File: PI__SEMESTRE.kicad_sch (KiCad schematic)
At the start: 30 parts, among them IC2 LMV358IDR, J1 CX90B-16P1, J3 Conn_01x04, SW1 SW_Boot, SW2 SW_Reset, U1 ESP32-S3-WROOM-1, U2 AMS1117, U5 GUVA-S12SD, U6 BME688

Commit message: cambios realizados para el esp32 s3 y unificacion de hojas
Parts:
- removed C1: TAJA106K016RNJ, TAJA106K016RNJ:CAPPM3216X180N, symbol TAJA106K016RNJ:TAJA106K016RNJ
- removed C2: TCJB226M025R0150E, TCJB226MO025R0150E:CAPPM3528X210N, symbol TCJB226M025R0150E:TCJB226M025R0150E
- added C1: 10u, symbol Device:C
- added C2: 100u, symbol Device:C
- added D2, D3: LED, LED_SMD:LED_1206_3216Metric, symbol Device:LED
- added R8, R9: 5.1KΩ, Resistor_SMD:R_0805_2012Metric, symbol Device:R
- C4: value 0.1uf -> 22u; footprint Capacitor_SMD:C_0201_0603Metric -> (none)
- C5: value 10uf -> 100n; footprint Capacitor_SMD:C_0402_1005Metric -> (none)
- R1, R2: footprint Resistor_SMD:R_0603_1608Metric_Pad0.98x0.95mm_HandSolder -> Resistor_SMD:R_0805_2012Metric
- R7: value 330Ω -> 5.1KΩ; footprint Resistor_SMD:R_0603_1608Metric_Pad0.98x0.95mm_HandSolder -> Resistor_SMD:R_0805_2012Metric
- U6: footprint Package_LGA:Bosch_LGA-8_3x3mm_P0.8mm_ClockwisePinNumbering -> BME688:IC_BME688
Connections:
- net +3.3V: now also C1.1, R8.2; no longer R7.2
- net +5V: now also R7.2, C2.1
- net GND: now also C1.2, C2.2, D2.1 (K), D3.1 (K)
- new net: D3.2 (A), R9.1
- new net: D2.2 (A), R8.1
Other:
- moved on the sheet: C3, J1, R1, R2, R3, R4, R5, SW2, U1

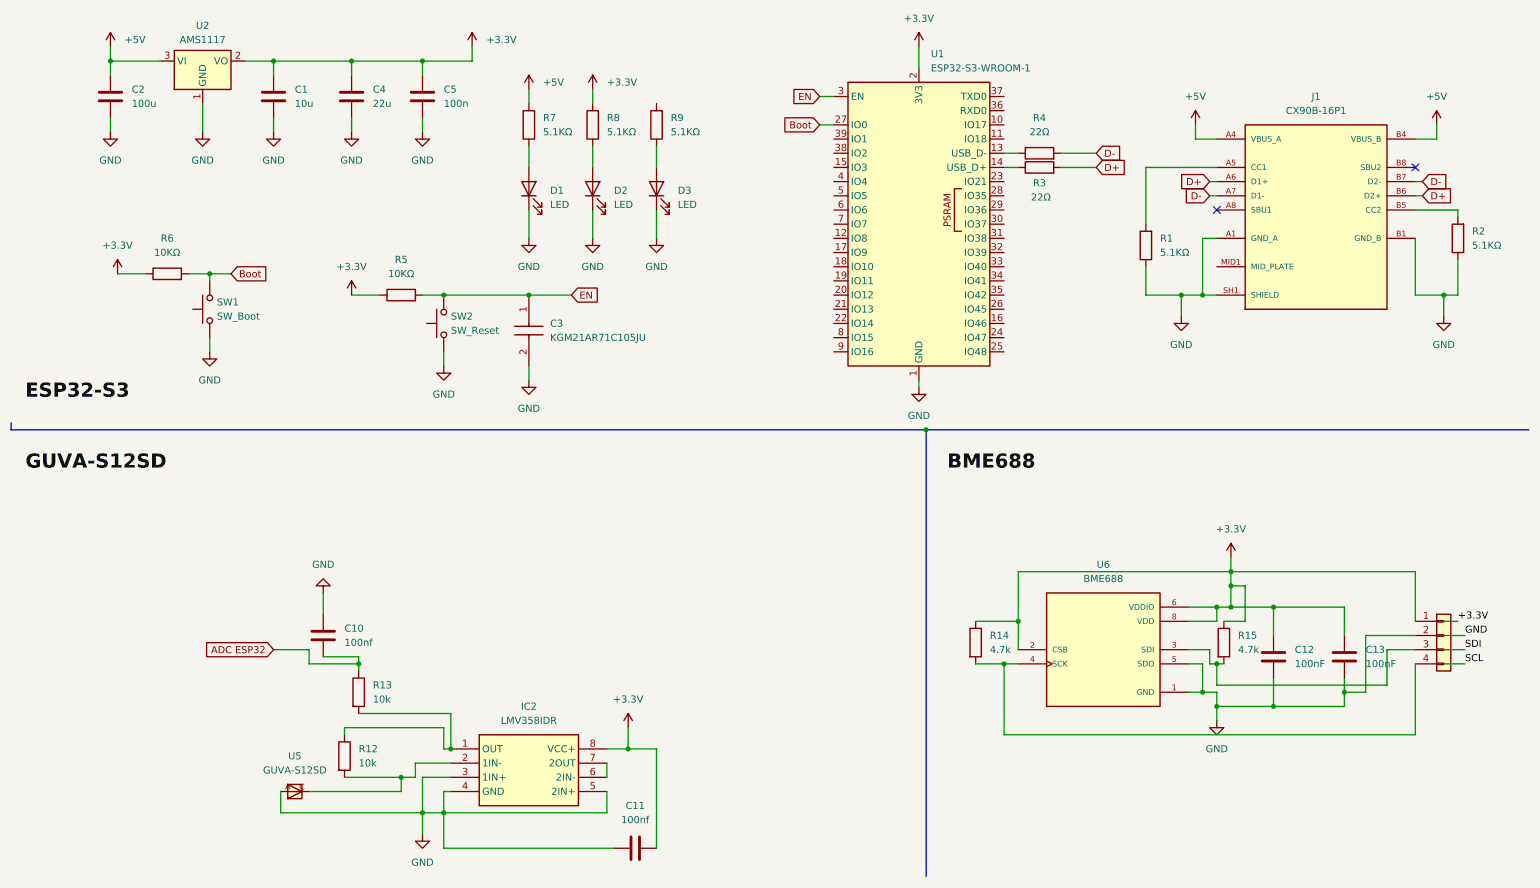
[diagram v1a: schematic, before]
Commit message: se corrige el esquematico del BME688 que sugirio el profesor, se le colocan etiquetas a las conexiones al esp32.
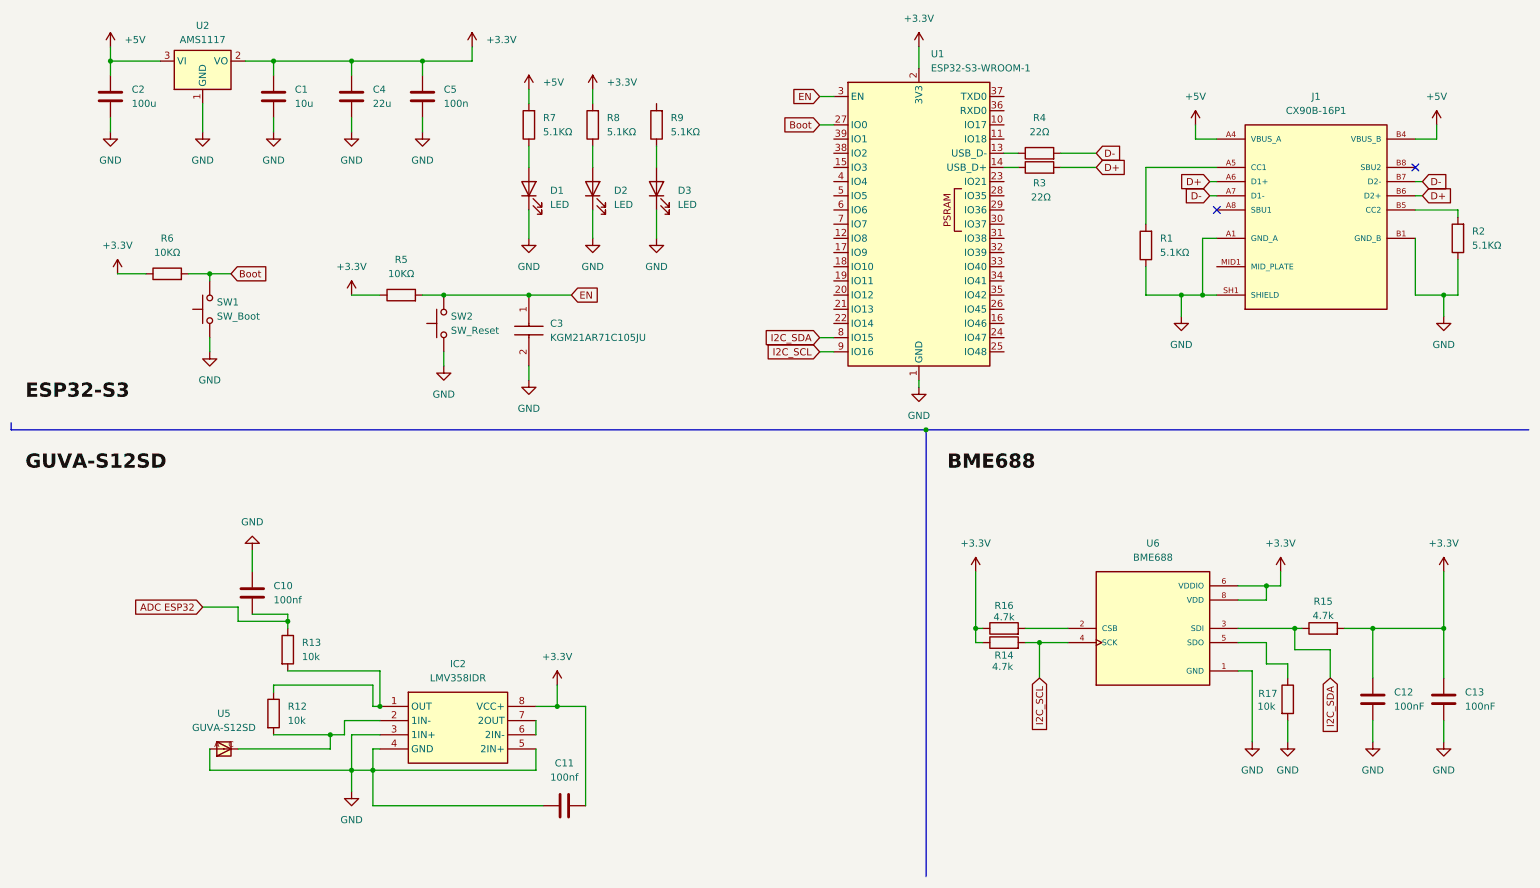
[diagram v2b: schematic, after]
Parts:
- removed J3: Conn_01x04, Connector_PinHeader_2.54mm:PinHeader_1x04_P2.54mm_Vertical, symbol Connector_Generic:Conn_01x04
- added R16: 4.7k, Resistor_SMD:R_0805_2012Metric, symbol Device:R
- added R17: 10k, Resistor_SMD:R_0805_2012Metric, symbol Device:R
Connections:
- net +3.3V: now also R15.2, R16.1; no longer R15.1, U6.2 (CSB)
- net GND: now also R17.2; no longer U6.5 (SDO)
- net I2C_SCL: now reaches R14.2, U6.4 (SCK)
- net I2C_SCL: now also U1.9 (IO16)
- net I2C_SDA: now reaches U1.8 (IO15)
- net I2C_SDA: now also R15.1, U6.3 (SDI)
- new net: R17.1, U6.5 (SDO)
- new net: R16.2, U6.2 (CSB)
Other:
- moved on the sheet: C10, C11, C12, C13, IC2, R12, R13, R14, R15, U5, U6

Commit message: se realizo los cambios que el profesor indico en la parte del guva s12sd, corrigiendo pistas, separando componentes y agregando el seguidor de voltaje que va desde nuestro filtro paso bajo hasta la esp 32 s3
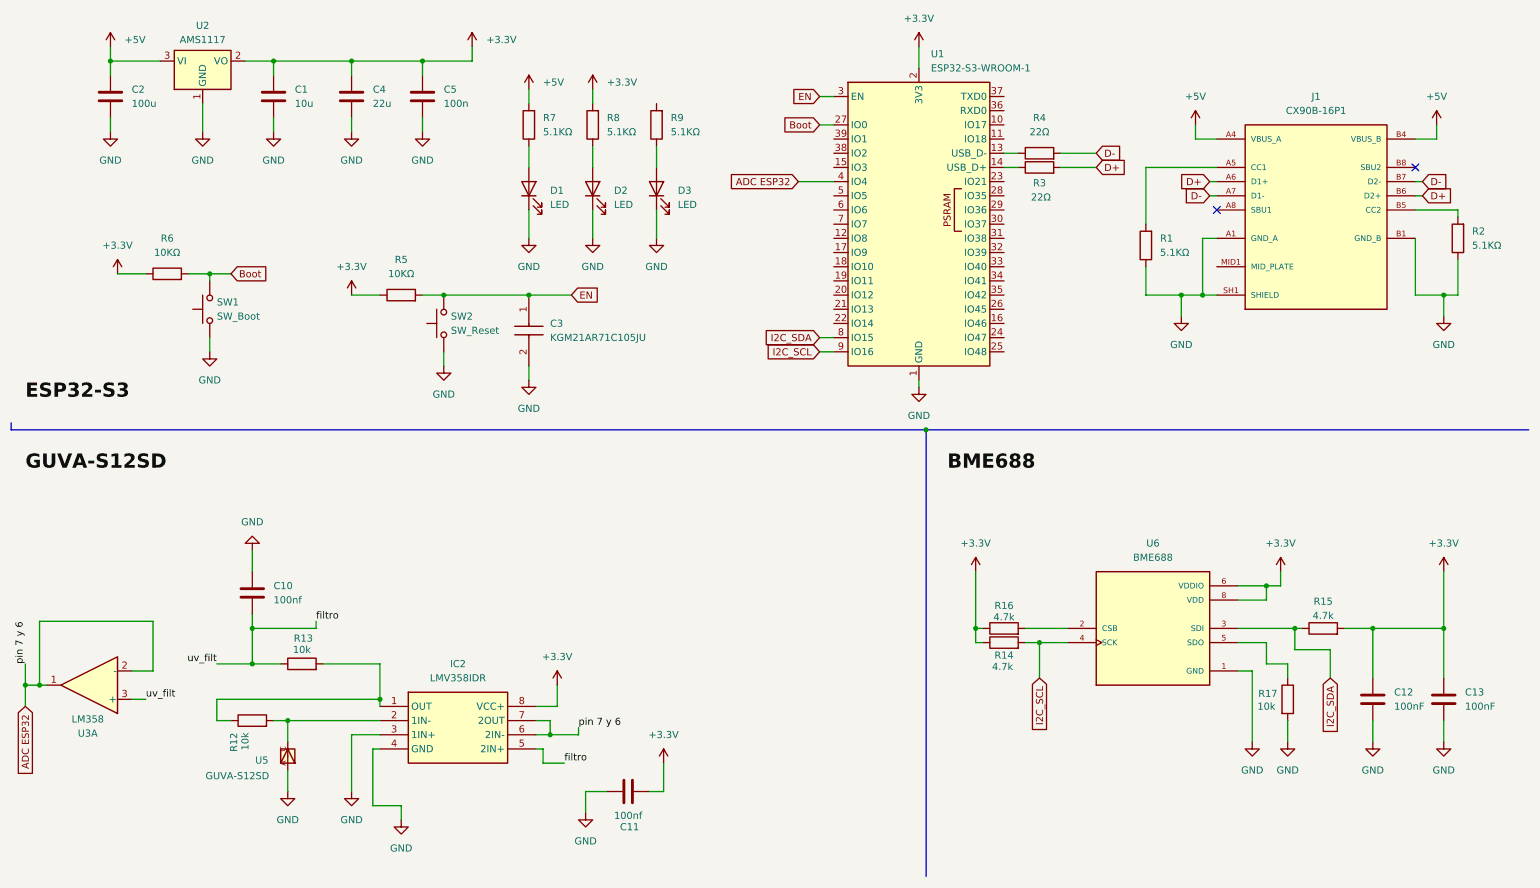
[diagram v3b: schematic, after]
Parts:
- added U3: LM358, symbol Amplifier_Operational:LM358
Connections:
- net ADC ESP32: now also IC2.6 (2IN-), IC2.7 (2OUT), U1.4 (IO4), U3.1, U3.2 (-); no longer C10.1, R13.1
- net GND: no longer IC2.5 (2IN+)
- new net filtro: C10.1, IC2.5 (2IN+), R13.1, U3.3 (+)
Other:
- moved on the sheet: C11, R12, R13, U5

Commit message: se implementan tanto huella y diseño 3D de los pulsadores booty reset, y tambien se le implementan la huella y diseño 3D a otros componentes como BME688, LMV358I, GUVA S12SD. se empieza a ordenar los componentes en el pcb
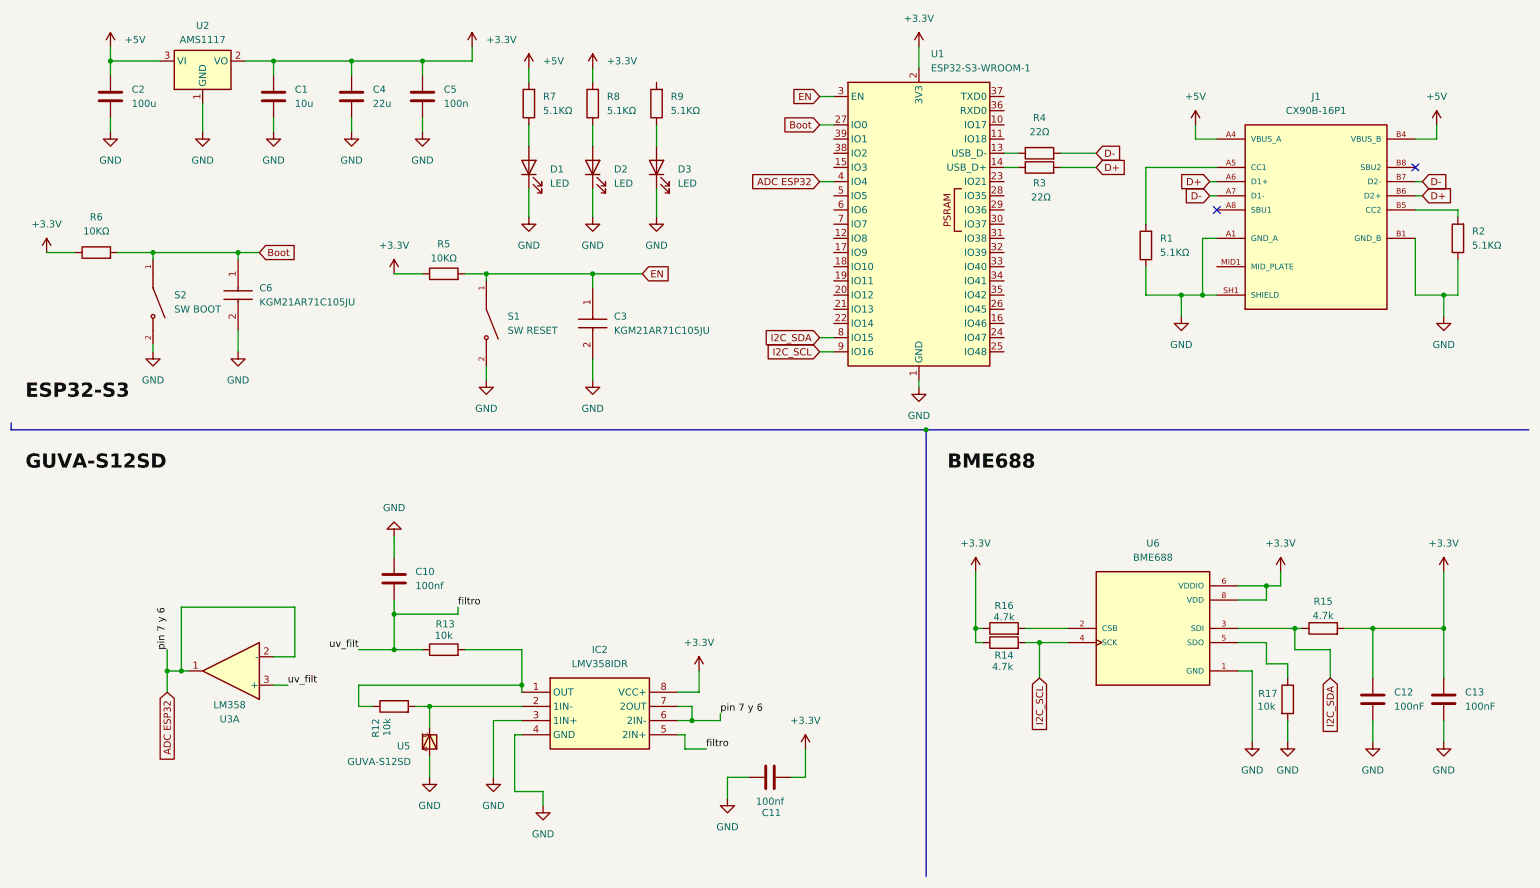
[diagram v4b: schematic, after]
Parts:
- removed SW1: SW_Boot, symbol Switch:SW_Push
- removed SW2: SW_Reset, symbol Switch:SW_Push
- added C6: KGM21AR71C105JU, CAPC2012X145N, symbol KGM21AR71C105JU:KGM21AR71C105JU
- added S1: SW RESET, TS-1088-AR02016:SW_TS-1088-AR02016, symbol TS-1088-AR02016:TS-1088-AR02016
- added S2: SW BOOT, TS-1088-AR02016:SW_TS-1088-AR02016, symbol TS-1088-AR02016:TS-1088-AR02016
- IC2: footprint LMV358IDR:SOIC127P600X175-8N -> LMV358I:SOIC127P600X175-8N
- U5: footprint GUVA-S12SD:GUVA-S12SD -> SamacSys_Parts:GUVA-S12SD
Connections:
- net Boot: now also C6.1, S2.1
- net EN: now also S1.1
- net GND: now also C6.2, S1.2, S2.2
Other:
- moved on the sheet: C10, C11, C3, D1, D2, D3, IC2, R12, R13, R5, R6, R7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

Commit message: se empieza a realizar el diseño para la pcb se dejan los componentes pocisionados para luego hacer las pistas, se rellena el contorno de la placa con conexion GND.
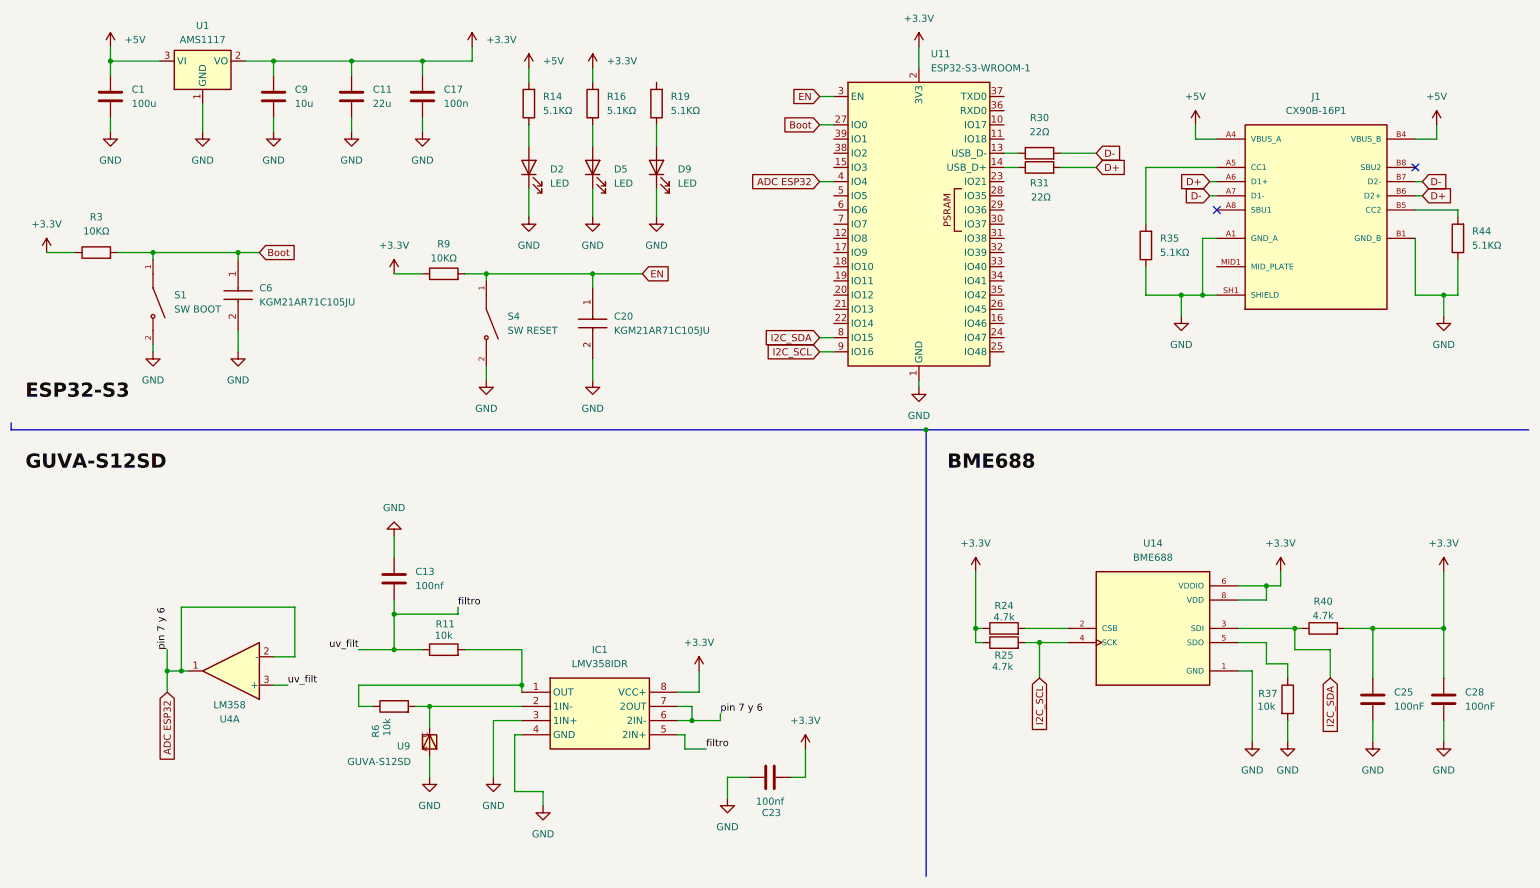
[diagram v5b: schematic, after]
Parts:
- R3: renamed from R6; footprint Resistor_SMD:R_0603_1608Metric_Pad0.98x0.95mm_HandSolder -> Resistor_SMD:R_0805_2012Metric
- R30: renamed from R4; footprint Resistor_SMD:R_0603_1608Metric_Pad0.98x0.95mm_HandSolder -> Resistor_SMD:R_0805_2012Metric
- R31: renamed from R3; footprint Resistor_SMD:R_0603_1608Metric_Pad0.98x0.95mm_HandSolder -> Resistor_SMD:R_0805_2012Metric
- R9: renamed from R5; footprint Resistor_SMD:R_0603_1608Metric_Pad0.98x0.95mm_HandSolder -> Resistor_SMD:R_0805_2012Metric
- U11: renamed from U1; footprint RF_Module:ESP32-S3-WROOM-1 -> SamacSys_Parts:XCVR_ESP32-S3-WROOM-1U-N16R8
- renumbered C2 to C1, C4 to C11, C10 to C13, C5 to C17, C3 to C20, C11 to C23, C12 to C25, C13 to C28, C1 to C9, D1 to D2, D2 to D5, D3 to D9, IC2 to IC1, R13 to R11, R7 to R14, R8 to R16, R9 to R19, R16 to R24, R14 to R25, R1 to R35, R17 to R37, R15 to R40, R2 to R44, R12 to R6, S2 to S1, S1 to S4, U2 to U1, U6 to U14, U3 to U4, U5 to U9

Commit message: algunas correcciones del profesor
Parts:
- removed U4: LM358, symbol Amplifier_Operational:LM358
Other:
- moved on the sheet: C23
